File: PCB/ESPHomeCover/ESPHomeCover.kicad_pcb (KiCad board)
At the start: 2 copper layers, 61 x 75 mm, 52 parts, among them IC1 ESP32-WROOM-32E-N4, J1 24V, J10 WINDOW, J3 I2C, J4 SPI, J5 Motor, J6 Brake, J8 Sensor UP, J9 Sensor DOWN, K1 G6S-2(F)-Y_DC24, Q1 MMBF170, U2 DRV8425PWPR, U3 AP63203WU-7, X2 Prog Header, Y1 32.768KHz

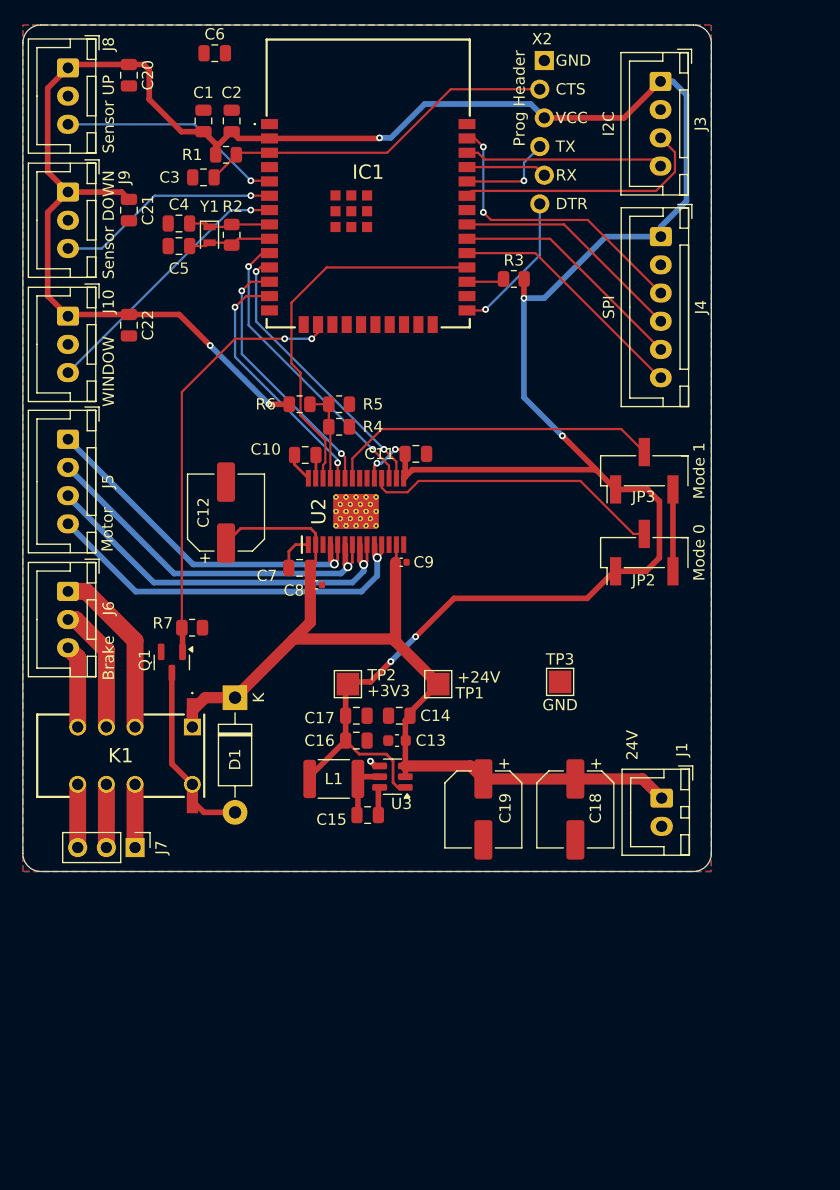
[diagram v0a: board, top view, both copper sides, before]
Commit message: small changes
change all Caps to 0603,
add bom
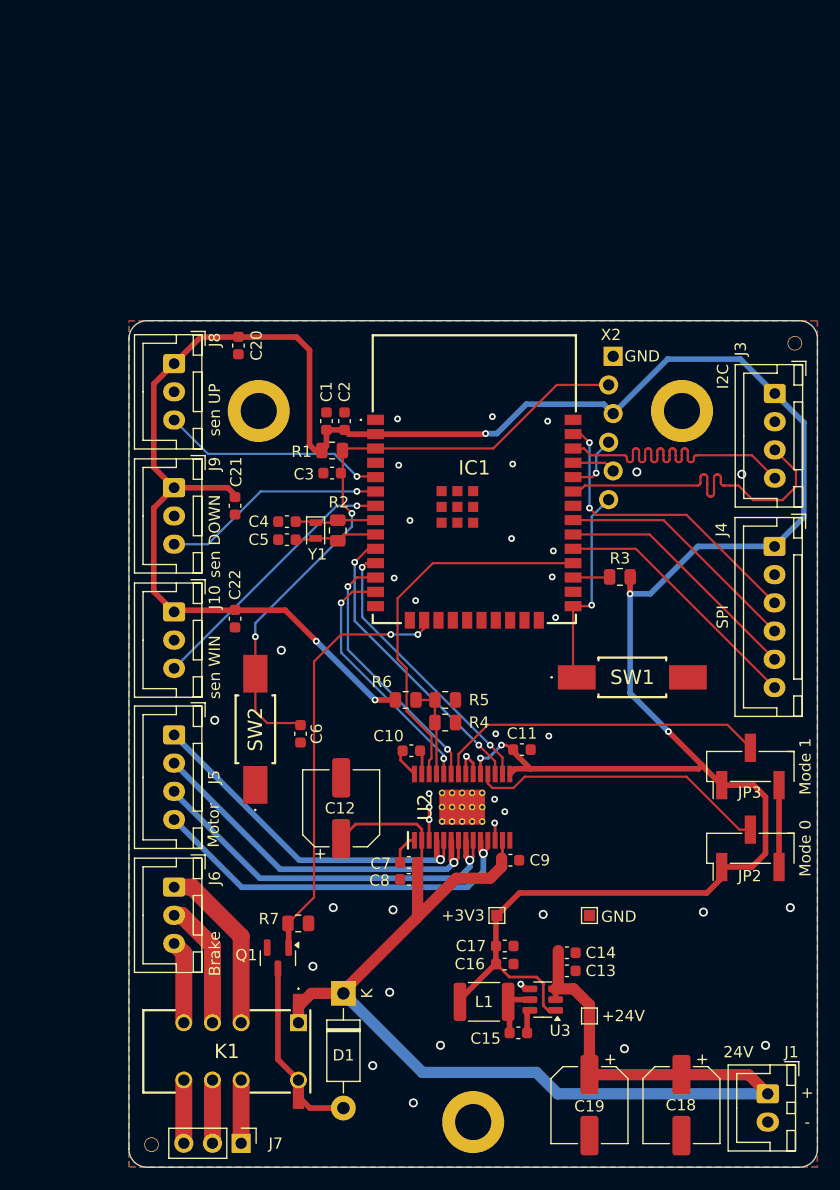
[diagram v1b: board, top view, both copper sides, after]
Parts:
- added H1: MountingHole_Pad, MountingHole:MountingHole_3.2mm_M3_ISO14580_Pad, F.Cu at (120.9, 69.2)
- added H2: MountingHole_Pad, MountingHole:MountingHole_3.2mm_M3_ISO14580_Pad, F.Cu at (158.4, 69.2)
- added H3: MountingHole_Pad, MountingHole:MountingHole_3.2mm_M3_ISO14580_Pad, F.Cu at (139.9, 132.2)
- added H4: tooling holes, Own_Lib:tooling holes, F.Cu at (111.4, 134.2)
- added H5: tooling holes, Own_Lib:tooling holes, F.Cu at (168.4, 63.2)
- added SW1: SW_BOOT, SamacSys_Parts:TL3302AF130QG, F.Cu at (154.0, 92.8)
- added SW2: SW_RESET, SamacSys_Parts:TL3302AF130QG, F.Cu at (120.6, 97.4)
- C1, C10, C11, C14, C15, C16, C17, C2, C20, C21, C22, C3, C4, C5, C6, C7: footprint Capacitor_SMD:C_0805_2012Metric -> Capacitor_SMD:C_0603_1608Metric
- C8, C9: footprint Capacitor_SMD:C_0402_1005Metric -> Capacitor_SMD:C_0603_1608Metric
- J10: value WINDOW -> sen WIN
- J8: value Sensor UP -> sen UP
- J9: value Sensor DOWN -> sen DOWN
- TP1, TP2, TP3: footprint TestPoint:TestPoint_Pad_2.0x2.0mm -> TestPoint:TestPoint_Pad_1.0x1.0mm
- moved C6 60.8 mm to (124.6, 97.8), turned to -90 degrees
- moved TP1 32.3 mm to (150.2, 122.8)
- moved J3 29.4 mm to (166.6, 67.7)
- moved J4 29.2 mm to (166.6, 81.2)
- moved C1 28.7 mm to (126.9, 70.1)
- moved C3 28.6 mm to (127.4, 74.7)
- moved C2 28.4 mm to (128.5, 70.1)
- moved C9 28.1 mm to (143.2, 109.0)
- moved C12 28.1 mm to (128.2, 104.4)
- moved C4 28.1 mm to (123.4, 79.0)
- moved R3 28.0 mm to (152.9, 83.9)
- moved D1 27.9 mm to (128.4, 120.8)
- moved C7 27.8 mm to (134.2, 109.2)
- moved J7 27.8 mm to (119.3, 134.1)
- moved C11 27.8 mm to (144.2, 99.2)
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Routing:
- net /Motor driver/+24V: track 88.2 -> 114.9 mm
- net /MCU/esp32_en: track 32.1 -> 57.1 mm, vias 0 -> 2
- net /MCU/I2C_SCL: track 17.6 -> 29.8 mm
- net GND: track 8.24 -> 16.1 mm, vias 1 -> 38
- net /MCU/I2C_SDA: track 22.9 -> 30.0 mm
- net /MCU/IO0/BOOT: track 13.0 -> 18.1 mm
- net Net-(IC1-RXD0): track 8.68 -> 5.38 mm
- net Net-(IC1-TXD0): track 7.15 -> 3.85 mm
- net /MCU/SPI_MISO: track 20.7 -> 21.9 mm
- net /MCU/SPI_CS: track 21.7 -> 22.9 mm
- net /MCU/SPI_MOSI: track 26.2 -> 27.4 mm
- net /MCU/SPI_CLK: track 21.2 -> 22.4 mm
- net Net-(U2-VCP): track 3.44 -> 2.74 mm
- net Net-(U3-SW): track 5.37 -> 4.81 mm
- net +3V3: track 252.4 -> 252.8 mm, vias 9 -> 7
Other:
- board text added: "+"
- board text added: "-"

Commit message: update PCB
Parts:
- added JP3: ~, Jumper:SolderJumper-2_P1.3mm_Open_RoundedPad1.0x1.5mm, F.Cu at (146.5, 111.9)
- J10: value sen WIN -> WIN
- J8: value sen UP -> UP
- J9: value sen DOWN -> DOWN
- moved C6 8.10 mm to (124.7, 89.7)
- moved SW1 0.30 mm to (154.0, 92.5)
- renumbered X2 to J1, J3 to J2, J4 to J3, J5 to J4, J6 to J5, J7 to J6, J1 to J7, JP2 to JP1, JP3 to JP2, U2 to U1, U3 to U2
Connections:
- C6 pad 1: /MCU/esp32_en -> GND
- C6 pad 2: GND -> /MCU/esp32_en
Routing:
- net /MCU/esp32_en: track 57.1 -> 54.3 mm
- net /MCU/brake_relay: track 38.0 -> 36.1 mm
- net Net-(J4-Pin_4): track 34.6 -> 35.6 mm
- net Net-(J4-Pin_3): track 34.2 -> 34.9 mm
- net Net-(J4-Pin_2): track 33.1 -> 33.7 mm
- net +3V3: track 252.8 -> 253.4 mm

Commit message: update PCB
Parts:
- turned C18 to 90 degrees
- turned C19 to 90 degrees
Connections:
- J7 pad 1: /Motor driver/+24V -> GND
- J7 pad 2: GND -> /Motor driver/+24V
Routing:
- net /Motor driver/+24V: track 114.9 -> 102.9 mm
- net GND: track 16.1 -> 17.8 mm, vias 38 -> 35
- net Net-(J4-Pin_4): track 35.6 -> 36.3 mm
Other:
- board text added: "${PROJECTNAME} Rev. ${REVISION} ${ISSUE_DATE}"

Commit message: update PCB
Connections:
- IC1 pad 24: unconnected-(IC1-IO2-Pad24) -> GND
